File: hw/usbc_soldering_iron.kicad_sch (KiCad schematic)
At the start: 85 parts, among them J1 U263-163N-4OS1735, J16 TIP_CONN, J2 DBG, J3 OLED, J4 GPIO, J5 DISP, Q1 AGM403AP, U1 SC7A20, U10 TPA191Ax, U2 CH32X035F8U6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

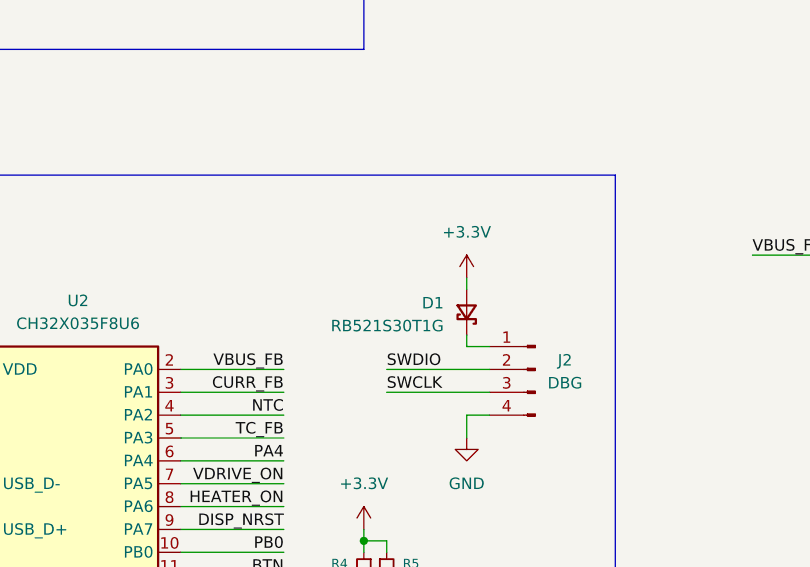
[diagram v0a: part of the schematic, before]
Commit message: removed diode in programming header
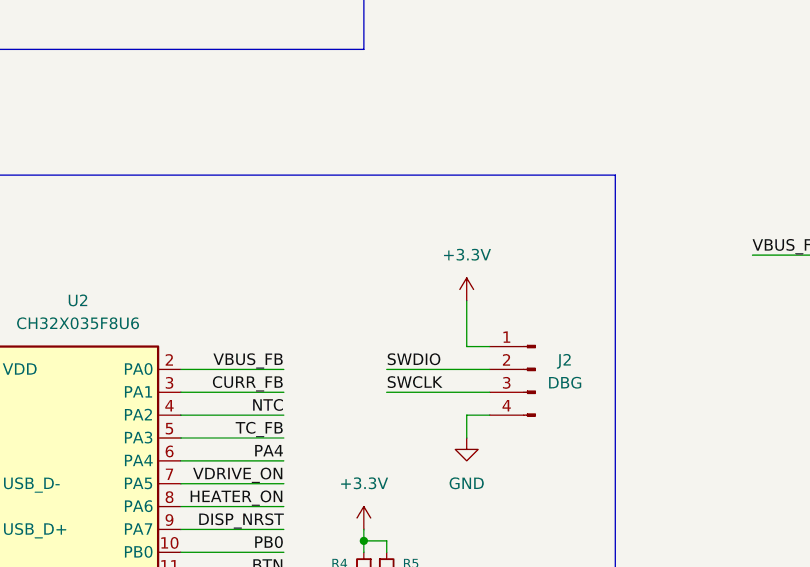
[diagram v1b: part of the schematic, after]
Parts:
- removed D1: RB521S30T1G, Diode_SMD:D_SOD-523, symbol Device:D_Schottky_Small
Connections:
- net +3.3V: now also J2.1 (Pin_1)
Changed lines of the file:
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@@
 	(wire
 		(pts
-			(xy 90.17 134.62) (xy 90.17 135.89)
+			(xy 90.17 130.81) (xy 90.17 135.89)
 		)
 		(stroke
@@
 	(wire
 		(pts
-			(xy 90.17 129.54) (xy 90.17 128.27)
-		)
-		(stroke
-			(width 0)
-			(type default)
-		)
-	)
-	(wire
-		(pts
 			(xy 78.74 156.21) (xy 78.74 157.48)
 		)
@@
 	(symbol
 		(lib_id "power:+3.3V")
-		(at 90.17 128.27 0)
+		(at 90.17 130.81 0)
 		(unit 1)
 		(body_style 1)
@@
 		(dnp no)
 		(property "Reference" "#PWR021"
-			(at 90.17 132.08 0)
+			(at 90.17 134.62 0)
 			(hide yes)
 			(show_name no)
@@
 		)
 		(property "Value" "+3.3V"
-			(at 90.17 123.19 0)
+			(at 90.17 125.73 0)
 			(show_name no)
 			(do_not_autoplace no)
@@
 		)
 		(property "Footprint" ""
-			(at 90.17 128.27 0)
+			(at 90.17 130.81 0)
 			(hide yes)
 			(show_name no)
@@
 		)
 		(property "Datasheet" ""
-			(at 90.17 128.27 0)
+			(at 90.17 130.81 0)
 			(hide yes)
 			(show_name no)
@@
 		)
 		(property "Description" "Power symbol creates a global label with name \"+3.3V\""
-			(at 90.17 128.27 0)
+			(at 90.17 130.81 0)
 			(hide yes)
 			(show_name no)
@@
 					(unit 1)
 				)
-			)
-		)
-	)
-	(symbol
-		(lib_id "Device:D_Schottky_Small")
-		(at 90.17 132.08 270)
-		(mirror x)
-		(unit 1)
-		(body_style 1)
-		(exclude_from_sim no)
-		(in_bom yes)
-		(on_board yes)
-		(in_pos_files yes)
-		(dnp no)
-		(property "Reference" "D1"
-			(at 87.63 131.0639 90)
-			(show_name no)
-			(do_not_autoplace no)
-			(effects
-				(font
-					(size 1.27 1.27)
-				)
-				(justify right)
-			)
-		)
-		(property "Value" "RB521S30T1G"
-			(at 87.63 133.6039 90)
-			(show_name no)
-			(do_not_autoplace no)
-			(effects
-				(font
-					(size 1.27 1.27)
-				)
-				(justify right)
-			)
-		)
-		(property "Footprint" "Diode_SMD:D_SOD-523"
-			(at 90.17 132.08 90)
-			(hide yes)
-			(show_name no)
-			(do_not_autoplace no)
-			(effects
-				(font
-					(size 1.27 1.27)
-				)
-			)
-		)
-		(property "Datasheet" ""
-			(at 90.17 132.08 90)
-			(hide yes)
-			(show_name no)
-			(do_not_autoplace no)
-			(effects
-				(font
-					(size 1.27 1.27)
-				)
-			)
-		)
-		(property "Description" "Schottky diode, small symbol"
-			(at 90.17 132.08 0)
-			(hide yes)
-			(show_name no)
-			(do_not_autoplace no)
-			(effects
-				(font
-					(size 1.27 1.27)
-				)
-			)
-		)
-		(pin "1"
-		)
-		(pin "2"
-		)
-		(instances
-			(project "usbc_soldering_iron"
-				(path "/7095b018-eac3-4b01-b374-28e3216c4fd8"
-					(reference "D1")
-					(unit 1)
-				)

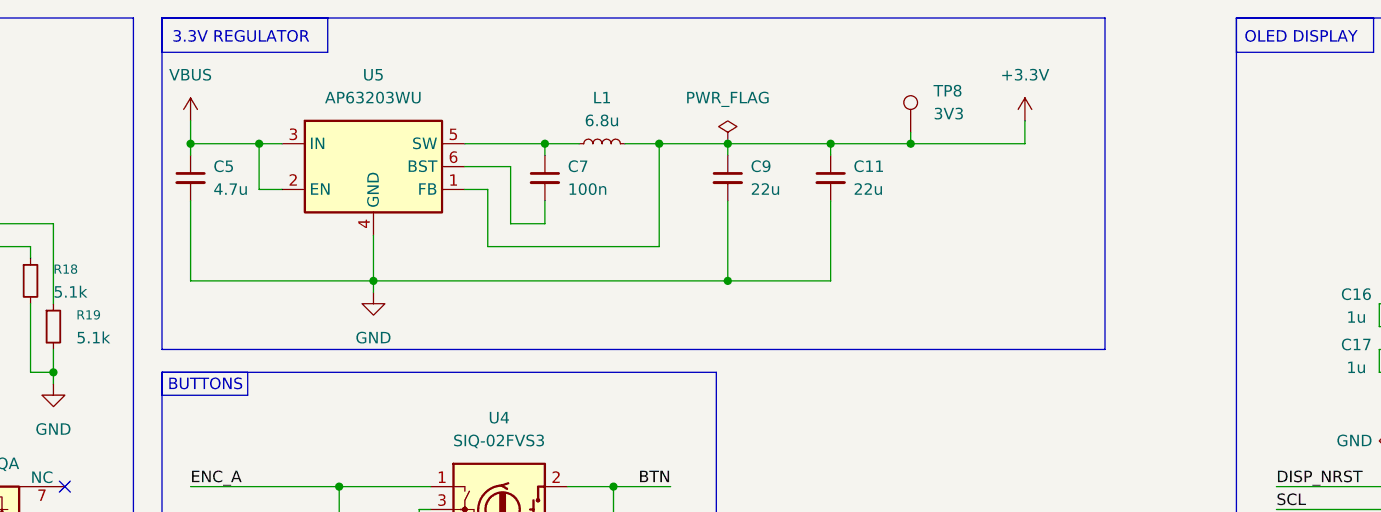
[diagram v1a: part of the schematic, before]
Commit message: more capacitors in main buck
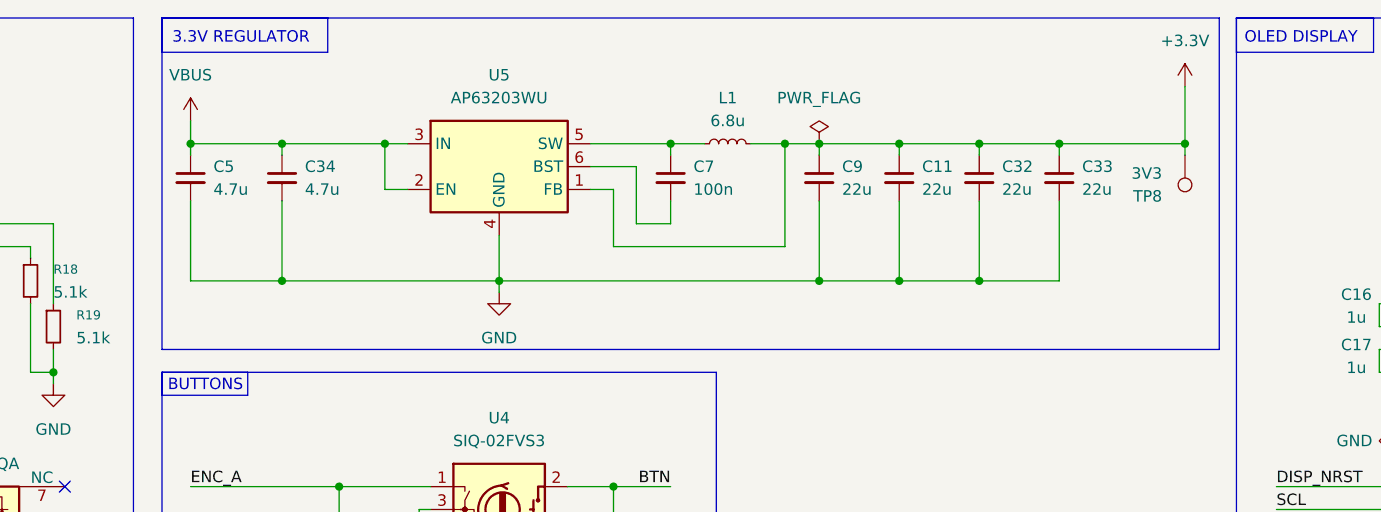
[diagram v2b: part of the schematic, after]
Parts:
- added C32, C33: 22u, Capacitor_SMD:C_0603_1608Metric, symbol Device:C_Small
- added C34: 4.7u, Capacitor_SMD:C_0805_2012Metric, symbol Device:C_Small
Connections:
- net +3.3V: now also C32.1, C33.1
- net GND: now also C32.2, C33.2, C34.2
- net VBUS: now also C34.1
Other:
- moved on the sheet: C11, C7, C9, L1, TP8, U5

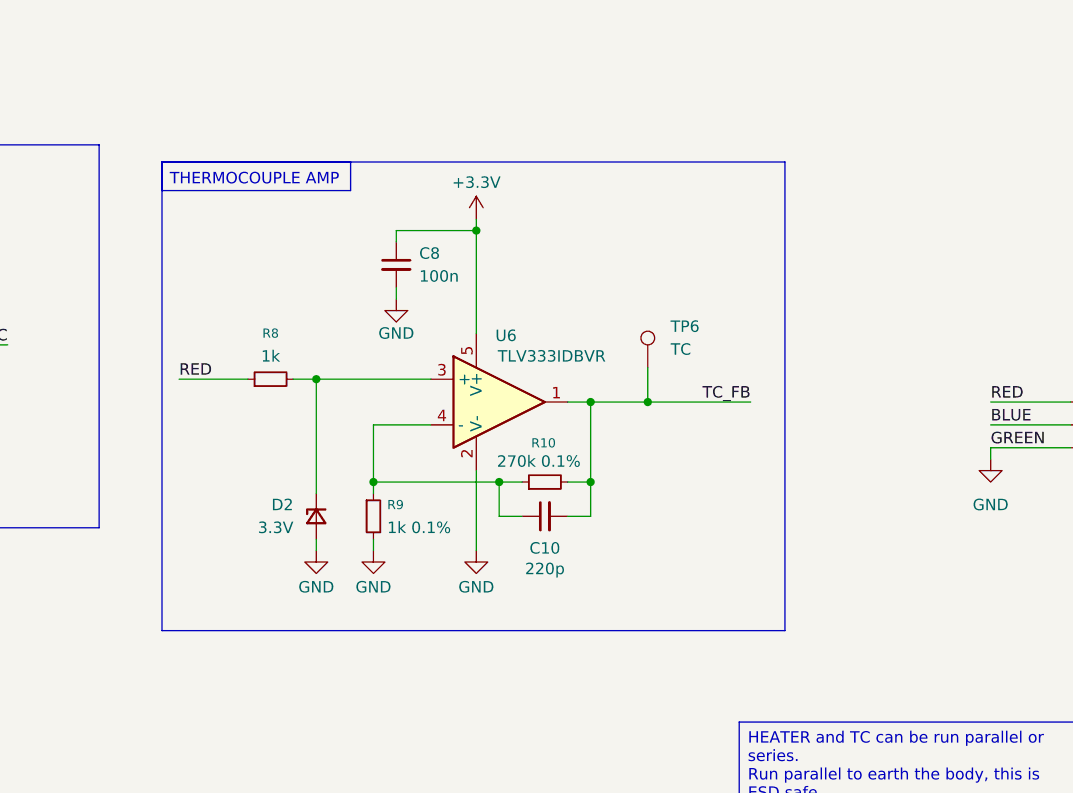
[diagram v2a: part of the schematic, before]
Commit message: better protection diode for tlv333
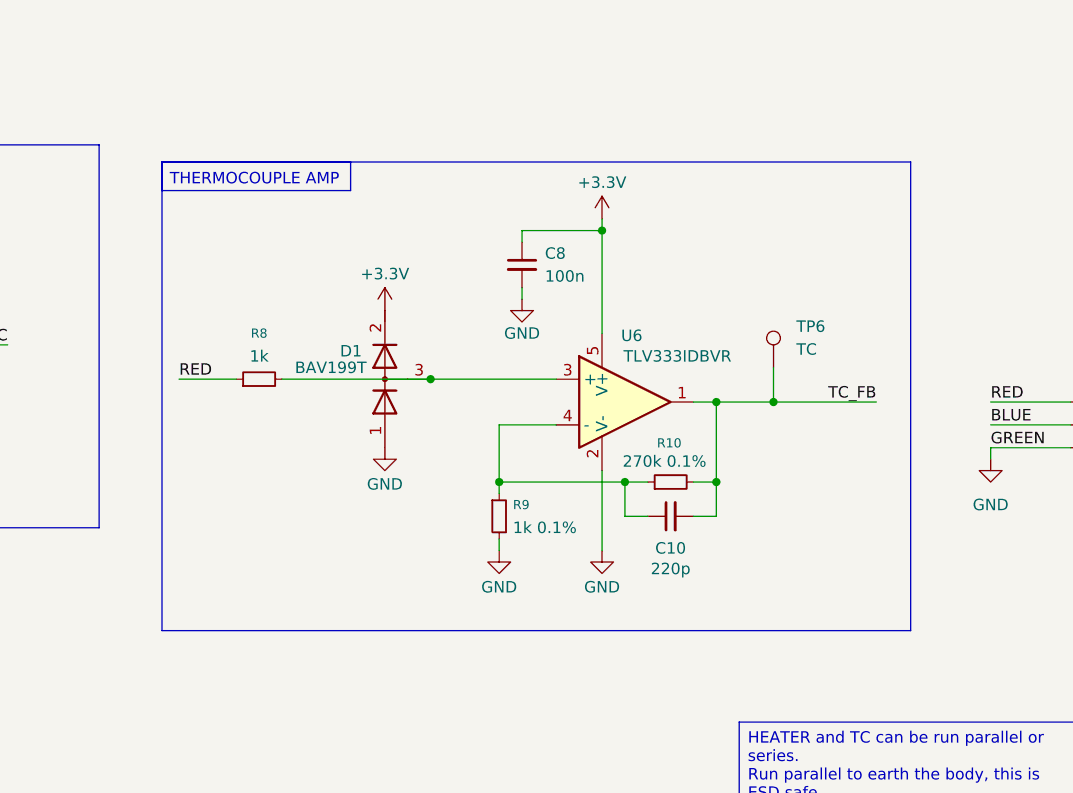
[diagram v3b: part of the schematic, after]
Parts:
- removed D2: 3.3V, Diode_SMD:D_SOD-523, symbol Device:D_Zener_Small
- added D1: BAV199T, Package_TO_SOT_SMD:SOT-523, symbol Device:D_Dual_Series_AKC
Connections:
- net +3.3V: now also D1.2 (K)
- net GND: now also D1.1 (A)
- net at R8.2, U6.3 (+): now also D1.3 (common)
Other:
- moved on the sheet: C10, C8, R10, R8, R9, TP6, U6

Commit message: new footprint for big inductor
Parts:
- L2: footprint Inductor_SMD:L_Changjiang_FNR4030S -> Custom:L_Changjiang_FNR4030S_Handsolder
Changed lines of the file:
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@@
 			)
 		)
-		(property "Footprint" "Inductor_SMD:L_Changjiang_FNR4030S"
+		(property "Footprint" "Custom:L_Changjiang_FNR4030S_Handsolder"
 			(at 223.52 114.3 0)
 			(hide yes)

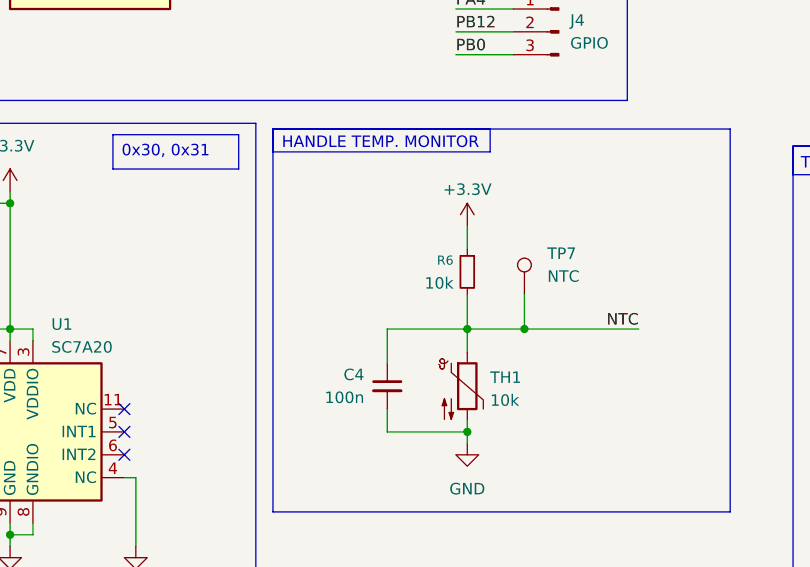
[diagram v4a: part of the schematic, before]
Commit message: lower tolerance in ntc pullup
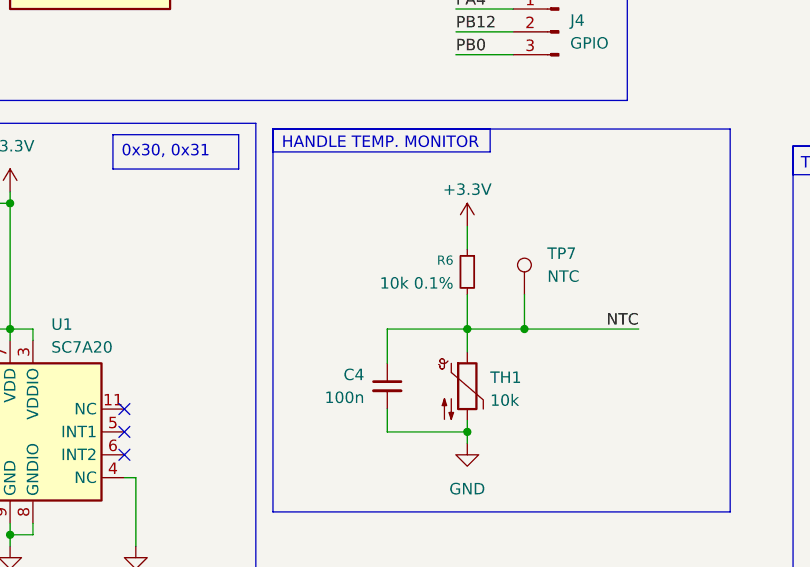
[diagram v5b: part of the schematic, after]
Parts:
- R6: value 10k -> 10k 0.1%
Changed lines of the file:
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@@
 			)
 		)
-		(property "Value" "10k"
+		(property "Value" "10k 0.1%"
 			(at 87.376 212.09 0)
 			(show_name no)

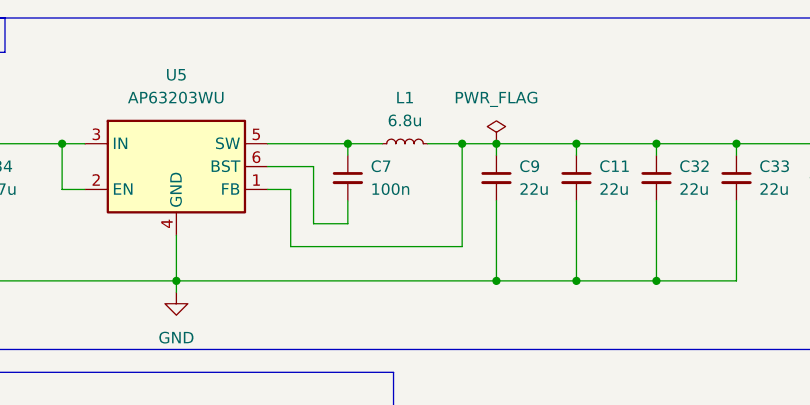
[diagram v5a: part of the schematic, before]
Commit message: different inductor
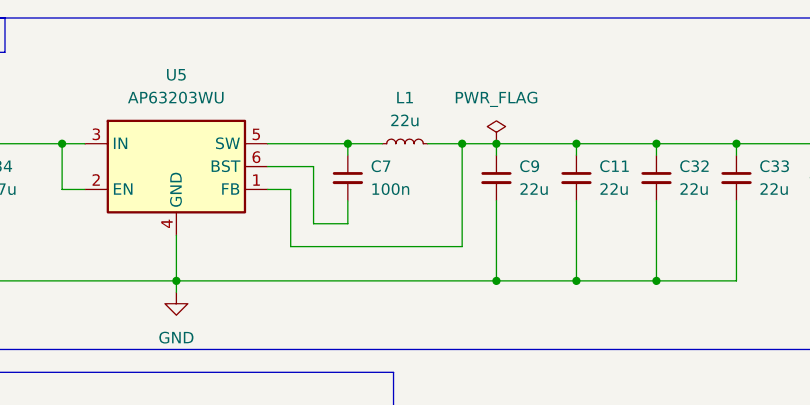
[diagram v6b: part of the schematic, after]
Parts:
- L1: value 6.8u -> 22u; footprint Inductor_SMD:L_Wuerth_MAPI-2010 -> Inductor_SMD:L_1210_3225Metric
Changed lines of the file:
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@@
 			)
 		)
-		(property "Value" "6.8u"
+		(property "Value" "22u"
 			(at 144.78 25.4 90)
 			(show_name no)
@@
 			)
 		)
-		(property "Footprint" "Inductor_SMD:L_Wuerth_MAPI-2010"
+		(property "Footprint" "Inductor_SMD:L_1210_3225Metric"
 			(at 144.78 27.94 0)
 			(hide yes)

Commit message: resistor tollerances
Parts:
- R16: value 10k -> 10k 0.1%
- R17: value 1k -> 1k 0.1%
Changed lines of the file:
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@@
 			)
 		)
-		(property "Value" "1k"
+		(property "Value" "1k 0.1%"
 			(at 136.906 130.81 0)
 			(show_name no)
@@
 			)
 		)
-		(property "Value" "10k"
+		(property "Value" "10k 0.1%"
 			(at 136.906 121.92 0)
 			(show_name no)

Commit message: started work on integrated pcb
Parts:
- removed H1, H2, H3, H4: MountingHole, MountingHole:MountingHole_2.2mm_M2_DIN965, symbol Mechanical:MountingHole
- removed J16: TIP_CONN, TerminalBlock_Phoenix:TerminalBlock_Phoenix_MKDS-1,5-3_1x03_P5.00mm_Horizontal, symbol Connector:Screw_Terminal_01x03
- removed J2: DBG, Connector_PinHeader_2.54mm:PinHeader_1x04_P2.54mm_Vertical, symbol Connector:Conn_01x04_Pin
- removed J4: GPIO, Connector_PinHeader_2.54mm:PinHeader_1x03_P2.54mm_Vertical, symbol Connector:Conn_01x03_Pin
- removed TP1: VBUS, TestPoint:TestPoint_Pad_D1.5mm, symbol Connector:TestPoint
- removed TP3: TIP, TestPoint:TestPoint_Pad_D1.5mm, symbol Connector:TestPoint
- removed TP4: DRIVE, TestPoint:TestPoint_Pad_D1.5mm, symbol Connector:TestPoint
- removed TP5: GATE, TestPoint:TestPoint_Pad_D1.5mm, symbol Connector:TestPoint
- removed TP6: TC, TestPoint:TestPoint_Pad_D1.5mm, symbol Connector:TestPoint
- removed TP7: NTC, TestPoint:TestPoint_Pad_D1.5mm, symbol Connector:TestPoint
- removed TP8: 3V3, TestPoint:TestPoint_Pad_D1.5mm, symbol Connector:TestPoint
- added J10, J11, J12, J13, J14, J15, J16, J17, J6, J7, J8, J9: Conn_01x01, Connector_Wire:SolderWire-1sqmm_1x01_D1.4mm_OD2.7mm, symbol Connector_Generic:Conn_01x01
- J1: footprint Custom:USB-C-SMD_U263-163N-4GS1735 -> Custom:USB-SMD_HC-TYPE-C-24P-CP1.0-5A-L10.45-01
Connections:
- net BLUE: now also J10.1 (Pin_1), J11.1 (Pin_1), J12.1 (Pin_1), J13.1 (Pin_1)
- net GND: now also J14.1 (Pin_1), J15.1 (Pin_1), J16.1 (Pin_1), J17.1 (Pin_1)
- net RED: now also J6.1 (Pin_1), J7.1 (Pin_1), J8.1 (Pin_1), J9.1 (Pin_1)
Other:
- moved on the sheet: C23, C24
